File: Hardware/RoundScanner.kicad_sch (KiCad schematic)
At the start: 0 parts

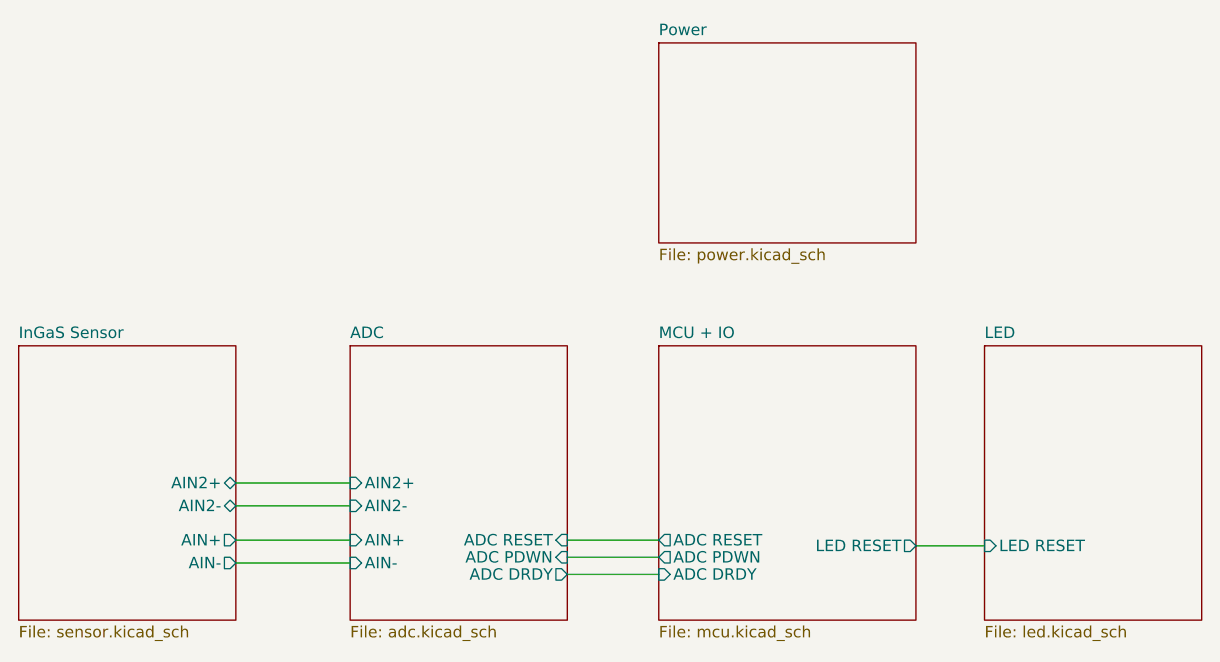
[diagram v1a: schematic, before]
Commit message: in the absence of design docs, I just did my own thing.  I've kept the ribbon cable, but I am not sure why there are one on either side, I've also brought out most of the interrupt lines on the through hole headers, the headers are designed for placement on a carrier board, negating the need for the ribbon cable when the board is stacked
Signed-off-by: lokimetasmith <lokimail@gmail.com>
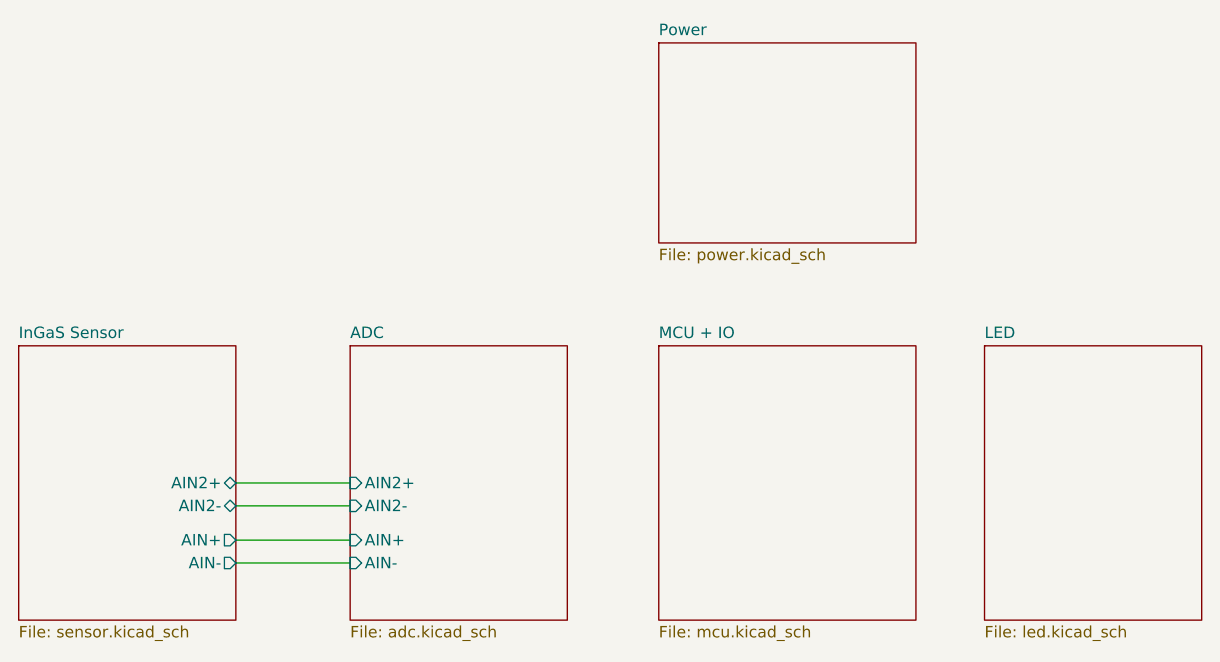
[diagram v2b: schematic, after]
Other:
- sheet ADC ports: added none; removed ADC DRDY, ADC PDWN, ADC RESET
- sheet LED ports: added none; removed LED RESET
- sheet MCU + IO ports: added none; removed ADC DRDY, ADC PDWN, ADC RESET, LED RESET
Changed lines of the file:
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@@
-    (stroke (width 0) (type default) (color 0 0 0 0))
-  )
-  (wire (pts (xy 129.54 99.06) (xy 139.7 99.06))
     (stroke (width 0) (type default) (color 0 0 0 0))
   )
@@
   )
   (wire (pts (xy 92.71 92.71) (xy 105.41 92.71))
-    (stroke (width 0) (type default) (color 0 0 0 0))
-  )
-  (wire (pts (xy 168.275 99.695) (xy 175.895 99.695))
-    (stroke (width 0) (type default) (color 0 0 0 0))
-  )
-  (wire (pts (xy 129.54 102.87) (xy 139.7 102.87))
-    (stroke (width 0) (type default) (color 0 0 0 0))
-  )
-  (wire (pts (xy 129.54 100.965) (xy 139.7 100.965))
     (stroke (width 0) (type default) (color 0 0 0 0))
   )
@@
       (effects (font (size 1.27 1.27)) (justify left top))
     )
-    (pin "LED RESET" input (at 175.895 99.695 180)
-      (effects (font (size 1.27 1.27)) (justify left))
-    )
   )
   (sheet (at 139.7 43.815) (size 28.575 22.225) (fields_autoplaced)
@@
       (effects (font (size 1.27 1.27)) (justify left))
     )
-    (pin "ADC RESET" input (at 129.54 99.06 0)
-      (effects (font (size 1.27 1.27)) (justify right))
-    )
-    (pin "ADC PDWN" input (at 129.54 100.965 0)
-      (effects (font (size 1.27 1.27)) (justify right))
-    )
-    (pin "ADC DRDY" output (at 129.54 102.87 0)
-      (effects (font (size 1.27 1.27)) (justify right))
-    )
     (pin "AIN2+" input (at 105.41 92.71 180)
       (effects (font (size 1.27 1.27)) (justify left))
@@
     (property "Sheet file" "mcu.kicad_sch" (id 1) (at 139.7 108.5346 0)
       (effects (font (size 1.27 1.27)) (justify left top))
-    )
-    (pin "ADC RESET" output (at 139.7 99.06 180)
-      (effects (font (size 1.27 1.27)) (justify left))
-    )
-    (pin "ADC PDWN" output (at 139.7 100.965 180)
-      (effects (font (size 1.27 1.27)) (justify left))
-    )
-    (pin "ADC DRDY" input (at 139.7 102.87 180)
-      (effects (font (size 1.27 1.27)) (justify left))
-    )
-    (pin "LED RESET" output (at 168.275 99.695 0)
-      (effects (font (size 1.27 1.27)) (justify right))
     )
   )
@@
       (reference "#PWR09") (unit 1) (value "GND") (footprint "")
     )
-    (path "/a8dcb7a4-48cf-403e-b881-d44234291c62/e83cfc6a-d9d2-4f41-9ed8-e16d04258196"
-      (reference "#PWR011") (unit 1) (value "GND") (footprint "")
+    (path "/5869e7b3-0d61-455b-97ad-e4e8b4829f27/6959919e-9236-44f6-bed8-c9993a6b48fa"
+      (reference "#PWR010") (unit 1) (value "GND") (footprint "")
     )
     (path "/a8dcb7a4-48cf-403e-b881-d44234291c62/51199e6d-598f-4680-8a1f-53cd14dedc18"
@@
       (reference "#PWR0132") (unit 1) (value "+3.3V") (footprint "")
     )
-    (path "/f3879066-a91b-415e-b241-18f9d05de4a2/b3d1803d-92bf-461d-bd0e-c894861ae3f7"
-      (reference "#PWR0133") (unit 1) (value "GND") (footprint "")
-    )
-    (path "/f3879066-a91b-415e-b241-18f9d05de4a2/04e8606e-e4f6-483c-9b64-a3c3b7a29ac4"
-      (reference "#PWR0134") (unit 1) (value "GND") (footprint "")
-    )
-    (path "/f3879066-a91b-415e-b241-18f9d05de4a2/66dbd06c-9ed1-44c9-b47a-57be7c411ac5"
-      (reference "#PWR0135") (unit 1) (value "GND") (footprint "")
+    (path "/a8dcb7a4-48cf-403e-b881-d44234291c62/7d5c9664-ce12-44c2-beef-3c42f0baca1f"
+      (reference "#PWR0133") (unit 1) (value "+3.3V") (footprint "")
     )
     (path "/98df1e87-3735-4cb9-8253-663f6eb2234f/fb03b7bb-2297-4d63-a835-8827b2d106f1"
@@
       (reference "C12") (unit 1) (value "51p") (footprint "Capacitor_SMD:C_0603_1608Metric_Pad1.08x0.95mm_HandSolder")
     )
+    (path "/a8dcb7a4-48cf-403e-b881-d44234291c62/badd1190-e6fc-4a06-8200-456cf48d10fd"
+      (reference "C13") (unit 1) (value "0.1uF") (footprint "Capacitor_SMD:C_0603_1608Metric_Pad1.08x0.95mm_HandSolder")
+    )
     (path "/5869e7b3-0d61-455b-97ad-e4e8b4829f27/c7c2250f-e41d-4b57-9778-aa463f2c204a"
       (reference "C14") (unit 1) (value "10uF") (footprint "Capacitor_SMD:C_0603_1608Metric_Pad1.08x0.95mm_HandSolder")
@@
       (reference "C23") (unit 1) (value "100p") (footprint "Capacitor_SMD:C_0603_1608Metric_Pad1.08x0.95mm_HandSolder")
     )
-    (path "/a8dcb7a4-48cf-403e-b881-d44234291c62/9039923c-dfbf-48e4-8eb9-bec6daedebcf"
-      (reference "C24") (unit 1) (value "18pF") (footprint "Capacitor_SMD:C_0603_1608Metric_Pad1.08x0.95mm_HandSolder")
-    )
-    (path "/a8dcb7a4-48cf-403e-b881-d44234291c62/22f293f6-8da2-41be-af38-4437d9ca0a6d"
-      (reference "C25") (unit 1) (value "18pF") (footprint "Capacitor_SMD:C_0603_1608Metric_Pad1.08x0.95mm_HandSolder")
-    )
     (path "/98df1e87-3735-4cb9-8253-663f6eb2234f/f05bbc97-e274-49a9-ab3b-42c85a8131c1"
       (reference "D1") (unit 1) (value "0090-3111-185") (footprint "Diode_SMD:D_1206_3216Metric_Pad1.42x1.75mm_HandSolder")
@@
       (reference "H2") (unit 1) (value "MountingHole") (footprint "MountingHole:MountingHole_2.2mm_M2_ISO7380_Pad")
     )
-    (path "/f3879066-a91b-415e-b241-18f9d05de4a2/6d6df775-4ba6-4706-8cd0-91175809d0ac"
-      (reference "H3") (unit 1) (value "MountingHole") (footprint "MountingHole:MountingHole_2.2mm_M2_ISO7380_Pad")
-    )
-    (path "/f3879066-a91b-415e-b241-18f9d05de4a2/983720b2-45fb-46e6-aa3e-98a2bd7cfb96"
-      (reference "H4") (unit 1) (value "MountingHole") (footprint "MountingHole:MountingHole_2.2mm_M2_ISO7380_Pad")
-    )
-    (path "/f3879066-a91b-415e-b241-18f9d05de4a2/40dc5062-01d4-4afd-b723-3edbebf43d5d"
-      (reference "H5") (unit 1) (value "MountingHole") (footprint "MountingHole:MountingHole_2.2mm_M2_ISO7380_Pad")
-    )
     (path "/5869e7b3-0d61-455b-97ad-e4e8b4829f27/e2f25370-b546-49d3-bdb0-cc886c2db087"
-      (reference "J1") (unit 1) (value "I2C Debug") (footprint "Connector_PinSocket_2.54mm:PinSocket_1x04_P2.54mm_Vertical")
+      (reference "J1") (unit 1) (value "I2C ThroughHole") (footprint "Connector_PinSocket_2.54mm:PinSocket_1x04_P2.54mm_Vertical")
     )
     (path "/5869e7b3-0d61-455b-97ad-e4e8b4829f27/574418b0-4eb3-4e5c-af93-568a8d0b32d5"
@@
       (reference "J3") (unit 1) (value "I2C") (footprint "Connector_JST:JST_SH_SM04B-SRSS-TB_1x04-1MP_P1.00mm_Horizontal")
     )
+    (path "/5869e7b3-0d61-455b-97ad-e4e8b4829f27/db0fcbe6-e44d-4ea8-b34b-36e63044e781"
+      (reference "J4") (unit 1) (value "Interface") (footprint "Connector_PinSocket_2.54mm:PinSocket_1x04_P2.54mm_Vertical")
+    )
     (path "/f3879066-a91b-415e-b241-18f9d05de4a2/7a211f01-92b2-485c-8073-e4a3611319d2"
       (reference "Q1") (unit 1) (value "BSS138DW-7-F") (footprint "BSS138DW-7-F-A:Diodes_Inc._-_BSS138DW-7-F-A")
@@
       (reference "R17") (unit 1) (value "51") (footprint "Resistor_SMD:R_0603_1608Metric_Pad0.98x0.95mm_HandSolder")
     )
-    (path "/a8dcb7a4-48cf-403e-b881-d44234291c62/4264af8b-a641-4e49-a1bf-294d02cb33e3"
-      (reference "R18") (unit 1) (value "270") (footprint "Resistor_SMD:R_0603_1608Metric_Pad0.98x0.95mm_HandSolder")
+    (path "/a8dcb7a4-48cf-403e-b881-d44234291c62/217bbbd3-3884-4c41-90f4-23f0b32095e9"
+      (reference "R18") (unit 1) (value "1k") (footprint "Resistor_SMD:R_0603_1608Metric_Pad0.98x0.95mm_HandSolder")
     )
     (path "/2f10b7a1-df61-45b4-9fd1-1ebf21b41a15/58bb65ca-65ad-4c40-9289-5cb34b09cd28"
@@
       (reference "R32") (unit 1) (value "82") (footprint "Resistor_SMD:R_0603_1608Metric_Pad0.98x0.95mm_HandSolder")
     )
+    (path "/5869e7b3-0d61-455b-97ad-e4e8b4829f27/80cc6b83-8eeb-4445-ba4e-d9f6e264c67c"
+      (reference "TP1") (unit 1) (value "Test_1.8V") (footprint "TestPoint:TestPoint_Pad_D1.5mm")
+    )
     (path "/2f10b7a1-df61-45b4-9fd1-1ebf21b41a15/4175082b-901c-45b8-bcd1-8484bd6045a5"
       (reference "TP3") (unit 1) (value "Test_3.3V") (footprint "TestPoint:TestPoint_Pad_D1.5mm")
@@
       (reference "U7") (unit 1) (value "AP7312-1833W6-7") (footprint "AP7312-1833W6-7:AP7312-1833W6-7")
     )
-    (path "/a8dcb7a4-48cf-403e-b881-d44234291c62/5a32c462-b5e8-4fff-8aec-2352f766b90d"
-      (reference "Y1") (unit 1) (value "Crystal_GND23") (footprint "Crystal:Crystal_SMD_HC49-SD")
-    )
-  )
+    (path "/a8dcb7a4-48cf-403e-b881-d44234291c62/66eb875f-e355-46dd-848b-6715376f0fa1"
+      (reference "X1") (unit 1) (value "SG-8002CE") (footprint "Oscillator:Oscillator_SMD_SeikoEpson_SG8002CE-4Pin_3.2x2.5mm")
+    )
+  )
